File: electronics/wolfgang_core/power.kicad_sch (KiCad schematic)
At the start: 25 parts, among them J1 Battery, J2 Power Supply, U1 LM5001MA, U2 ACS724xLCTR-50AB, U3 LTC4418IUF-PBF

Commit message: More work on CORE Rev2
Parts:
- removed D7: STPS60L30CW, symbol Device:D_Schottky_Dual_CommonCathode_AAK_Parallel
- added C11, C12, C13, C14, C15, C8: C_Small, symbol Device:C_Small
- added C5, C6, C7: C_Polarized_Small, symbol Device:C_Polarized_Small
- added Q1, Q2, Q3, Q4: SUM110P06-08L-E3, symbol Simulation_SPICE:PMOS
- added R11, R12, R13: R_Small, symbol Device:R_Small
- renumbered J2 to J1, J1 to J2
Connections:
- net GND: now also U3.21 (GND), U3.8 (GND), C11.2, C12.2, C13.2, C14.2, C15.2, C5.2, C6.2, C7.2, C8.2, R13.2
- net v_bat: now also R9.1, U3.16 (V2), C7.1, C8.1, Q3.1 (D)
- net v_ext: now also R5.1, U3.17 (V1), C11.1, C6.1, Q1.1 (D)
- net at F1.1: now also U3.15 (V_{OUT}), C5.1, Q2.3 (S), Q4.3 (S), R11.1, R12.1
- net at U3.1 (TMR): now also C14.1
- net at U3.10 (INTV_{CC}): now also U3.18 (EN), U3.9 (CAS), C15.1
- net at U3.11 (G2): now also Q3.2 (G), Q4.2 (G)
- net at U3.12 (VS2): now also C13.1, Q3.3 (S), Q4.1 (D)
- net at U3.13 (G1): now also Q1.2 (G), Q2.2 (G)
- net at U3.14 (VS1): now also C12.1, Q1.3 (S), Q2.1 (D)
- net at U3.20 (HYS): now also R13.1
- net at U3.6 (~{VALID1}): now also R11.2
- net at U3.7 (~{VALID2}): now also R12.2
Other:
- note added: "Note: When contiiung to copy the design, make sure to copy e.g. Figure 10 so that both inputs are hotswappable."
- note added: "TODO: find correct values of the resistors around the LTC44418IUF"
- note removed: "replace with ltc4418"
- moved on the sheet: C1, C10, C2, C3, C4, C9, D8, F1, J1, J2, L1, R1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

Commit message: Further WIP on Power Rev 2.0
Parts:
- C14: value C_Small -> 1nF
- R10, R6: value R_Small -> 2k
- R13: value R_Small -> 0
- R5, R9: value R_Small -> 18k
- R7, R8: value R_Small -> 1k
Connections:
- net GND: now also R7.1, R8.1
- net at C15.1, U3.10 (INTV_{CC}), U3.18 (EN): now also U3.19 (~{SHDN}); no longer U3.9 (CAS)
- no-connect marks 1 -> 2
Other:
- note added: "Note: When continuiung to copy the design, make sure to copy e.g. Figure 10 so that both inputs are hotswappable."
- note added: "Values for V-Div from CIT team. Motivation for exact values unknown They will work, but examples in the datasheet are always a lot bgger (e.g. R5=R9=1M Ohm)"
- note removed: "Note: When contiiung to copy the design, make sure to copy e.g. Figure 10 so that both inputs are hotswappable."
- note removed: "TODO: find correct values of the resistors around the LTC44418IUF"
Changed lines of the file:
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@@
 	)
 	(junction
-		(at 125.73 88.9)
-		(diameter 0)
-		(color 0 0 0 0)
-	)
-	(junction
 		(at 105.41 49.53)
 		(diameter 0)
@@
 	)
 	(junction
-		(at 125.73 85.09)
-		(diameter 0)
-		(color 0 0 0 0)
-	)
-	(junction
 		(at 88.9 186.69)
 		(diameter 0)
@@
 	)
 	(junction
+		(at 125.73 88.9)
+		(diameter 0)
+		(color 0 0 0 0)
+	)
+	(junction
 		(at 270.51 57.15)
 		(diameter 0)
@@
 	)
 	(junction
+		(at 125.73 92.71)
+		(diameter 0)
+		(color 0 0 0 0)
+	)
+	(junction
 		(at 124.46 138.43)
 		(diameter 0)
@@
 		(at 66.04 165.1)
 	)
+	(no_connect
+		(at 125.73 85.09)
+	)
 	(wire
 		(pts
@@
 	(wire
 		(pts
+			(xy 125.73 88.9) (xy 140.97 88.9)
+		)
+		(stroke
+			(width 0)
+			(type default)
+		)
+	)
+	(wire
+		(pts
 			(xy 102.87 114.3) (xy 107.95 114.3)
 		)
@@
 	(wire
 		(pts
+			(xy 140.97 96.52) (xy 140.97 88.9)
+		)
+		(stroke
+			(width 0)
+			(type default)
+		)
+	)
+	(wire
+		(pts
 			(xy 160.02 71.12) (xy 160.02 63.5)
 		)
@@
 	(wire
 		(pts
-			(xy 140.97 85.09) (xy 125.73 85.09)
-		)
-		(stroke
-			(width 0)
-			(type default)
-		)
-	)
-	(wire
-		(pts
 			(xy 134.62 45.72) (xy 140.97 45.72)
 		)
@@
 	(wire
 		(pts
-			(xy 125.73 85.09) (xy 125.73 88.9)
-		)
-		(stroke
-			(width 0)
-			(type default)
-		)
-	)
-	(wire
-		(pts
 			(xy 96.52 138.43) (xy 106.68 138.43)
 		)
@@
 	(wire
 		(pts
-			(xy 124.46 96.52) (xy 125.73 96.52)
+			(xy 246.38 71.12) (xy 247.65 71.12)
 		)
 		(stroke
@@
 	(wire
 		(pts
-			(xy 246.38 71.12) (xy 247.65 71.12)
+			(xy 29.21 25.4) (xy 58.42 25.4)
 		)
 		(stroke
@@
 	(wire
 		(pts
-			(xy 29.21 25.4) (xy 58.42 25.4)
+			(xy 80.01 138.43) (xy 88.9 138.43)
 		)
 		(stroke
@@
 	(wire
 		(pts
-			(xy 80.01 138.43) (xy 88.9 138.43)
+			(xy 87.63 44.45) (xy 87.63 58.42)
 		)
 		(stroke
@@
 	(wire
 		(pts
-			(xy 87.63 44.45) (xy 87.63 58.42)
+			(xy 91.44 109.22) (xy 91.44 114.3)
 		)
 		(stroke
@@
 	(wire
 		(pts
-			(xy 91.44 109.22) (xy 91.44 114.3)
+			(xy 160.02 63.5) (xy 160.02 38.1)
 		)
 		(stroke
@@
 	(wire
 		(pts
-			(xy 160.02 63.5) (xy 160.02 38.1)
+			(xy 125.73 92.71) (xy 125.73 96.52)
 		)
 		(stroke
@@
 	(wire
 		(pts
-			(xy 140.97 96.52) (xy 140.97 85.09)
-		)
-		(stroke
-			(width 0)
-			(type default)
-		)
-	)
-	(wire
-		(pts
 			(xy 146.05 38.1) (xy 160.02 38.1)
 		)
@@
 		)
 	)
-	(text "TODO: find correct values of the resistors around the LTC44418IUF"
+	(text "Supply Selection"
 		(exclude_from_sim no)
-		(at 84.328 124.206 0)
+		(at 59.182 16.51 0)
 		(effects
 			(font
@@
 		)
 	)
-	(text "Supply Selection"
+	(text "Mini ATO Fuse"
 		(exclude_from_sim no)
-		(at 59.182 16.51 0)
+		(at 229.616 29.21 0)
 		(effects
 			(font
@@
 		)
 	)
-	(text "Mini ATO Fuse"
+	(text "Values for V-Div from CIT team.\nMotivation for exact values unknown\nThey will work, but examples in\nthe datasheet are always a lot\nbgger (e.g. R5=R9=1M Ohm)"
 		(exclude_from_sim no)
-		(at 229.616 29.21 0)
+		(at 33.02 84.582 0)
 		(effects
 			(font
@@
 		)
 	)
-	(text "Note: When contiiung to copy the design, make sure to copy e.g. Figure 10 so that both inputs are hotswappable."
+	(text "Note: When continuiung to copy the design, make sure to copy e.g. Figure 10 so that both inputs are hotswappable."
 		(exclude_from_sim no)
 		(at 106.426 126.746 0)
@@
 	)
 	(symbol
+		(lib_id "power:GND")
+		(at 53.34 97.79 270)
+		(unit 1)
+		(exclude_from_sim no)
+		(in_bom yes)
+		(on_board yes)
+		(dnp no)
+		(fields_autoplaced yes)
+		(property "Reference" "#PWR036"
+			(at 46.99 97.79 0)
+			(effects
+				(font
+					(size 1.27 1.27)
+				)
+				(hide yes)
+			)
+		)
+		(property "Value" "GND"
+			(at 49.53 97.7899 90)
+			(effects
+				(font
+					(size 1.27 1.27)
+				)
+				(justify right)
+			)
+		)
+		(property "Footprint" ""
+			(at 53.34 97.79 0)
+			(effects
+				(font
+					(size 1.27 1.27)
+				)
+				(hide yes)
+			)
+		)
+		(property "Datasheet" ""
+			(at 53.34 97.79 0)
+			(effects
+				(font
+					(size 1.27 1.27)
+				)
+				(hide yes)
+			)
+		)
+		(property "Description" "Power symbol creates a global label with name \"GND\" , ground"
+			(at 53.34 97.79 0)
+			(effects
+				(font
+					(size 1.27 1.27)
+				)
+				(hide yes)
+			)
+		)
+		(pin "1"
+		)
+		(instances
+			(project "wolfgang_core"
+				(path "/9538e4ed-27e6-4c37-b989-9859dc0d49e8/03085433-09a6-46e6-a151-340cb0e29306"
+					(reference "#PWR036")
+					(unit 1)
+				)
+			)
+		)
+	)
+	(symbol
 		(lib_id "Connector_Generic:Conn_01x02")
 		(at 24.13 40.64 0)
@@
 			)
 		)
-		(property "Value" "R_Small"
+		(property "Value" "1k"
 			(at 69.85 83.312 90)
 			(effects
@@
 			)
 		)
-		(property "Value" "R_Small"
+		(property "Value" "18k"
 			(at 61.976 90.17 0)
 			(effects
@@
 			)
 		)
-		(property "Value" "R_Small"
+		(property "Value" "2k"
 			(at 75.946 78.74 0)
 			(effects
@@
 			)
 		)
-		(property "Value" "R_Small"
+		(property "Value" "2k"
 			(at 61.976 95.25 0)
 			(effects
@@
 			)
 		)
-		(property "Value" "R_Small"
+		(property "Value" "18k"
 			(at 75.946 73.66 0)
 			(effects
@@
 	(symbol
 		(lib_id "power:GND")
+		(at 67.31 81.28 270)
+		(unit 1)
+		(exclude_from_sim no)
+		(in_bom yes)
+		(on_board yes)
+		(dnp no)
+		(fields_autoplaced yes)
+		(property "Reference" "#PWR035"
+			(at 60.96 81.28 0)
+			(effects
+				(font
+					(size 1.27 1.27)
+				)
+				(hide yes)
+			)
+		)
+		(property "Value" "GND"
+			(at 63.5 81.2799 90)
+			(effects
+				(font
+					(size 1.27 1.27)
+				)
+				(justify right)
+			)
+		)
+		(property "Footprint" ""
+			(at 67.31 81.28 0)
+			(effects
+				(font
+					(size 1.27 1.27)
+				)
+				(hide yes)
+			)
+		)
+		(property "Datasheet" ""
+			(at 67.31 81.28 0)
+			(effects
+				(font
+					(size 1.27 1.27)
+				)
+				(hide yes)
+			)
+		)
+		(property "Description" "Power symbol creates a global label with name \"GND\" , ground"
+			(at 67.31 81.28 0)
+			(effects
+				(font
+					(size 1.27 1.27)
+				)
+				(hide yes)
+			)
+		)
+		(pin "1"
+		)
+		(instances
+			(project "wolfgang_core"
+				(path "/9538e4ed-27e6-4c37-b989-9859dc0d49e8/03085433-09a6-46e6-a151-340cb0e29306"
+					(reference "#PWR035")
+					(unit 1)
+				)
+			)
+		)
+	)
+	(symbol
+		(lib_id "power:GND")
 		(at 72.39 58.42 0)
 		(unit 1)
@@
 		(on_board yes)
 		(dnp no)
-		(fields_autoplaced yes)
 		(property "Reference" "C14"
-			(at 110.49 110.4962 0)
+			(at 108.712 109.982 0)
 			(effects
 				(font
@@
 			)
 		)
-		(property "Value" "C_Small"
-			(at 110.49 113.0362 0)
+		(property "Value" "1nF"
+			(at 108.966 113.03 0)
 			(effects
 				(font
@@
 		(on_board yes)
 		(dnp no)
-		(fields_autoplaced yes)
 		(property "Reference" "R13"
-			(at 105.41 110.4899 0)
+			(at 100.838 113.792 90)
 			(effects
 				(font
@@
 			)
 		)
-		(property "Value" "R_Small"
-			(at 105.41 113.0299 0)
+		(property "Value" "0"
+			(at 104.902 113.792 90)
 			(effects
 				(font
@@
 			)
 		)
-		(property "Value" "R_Small"
+		(property "Value" "1k"
 			(at 55.88 99.822 90)
 			(effects

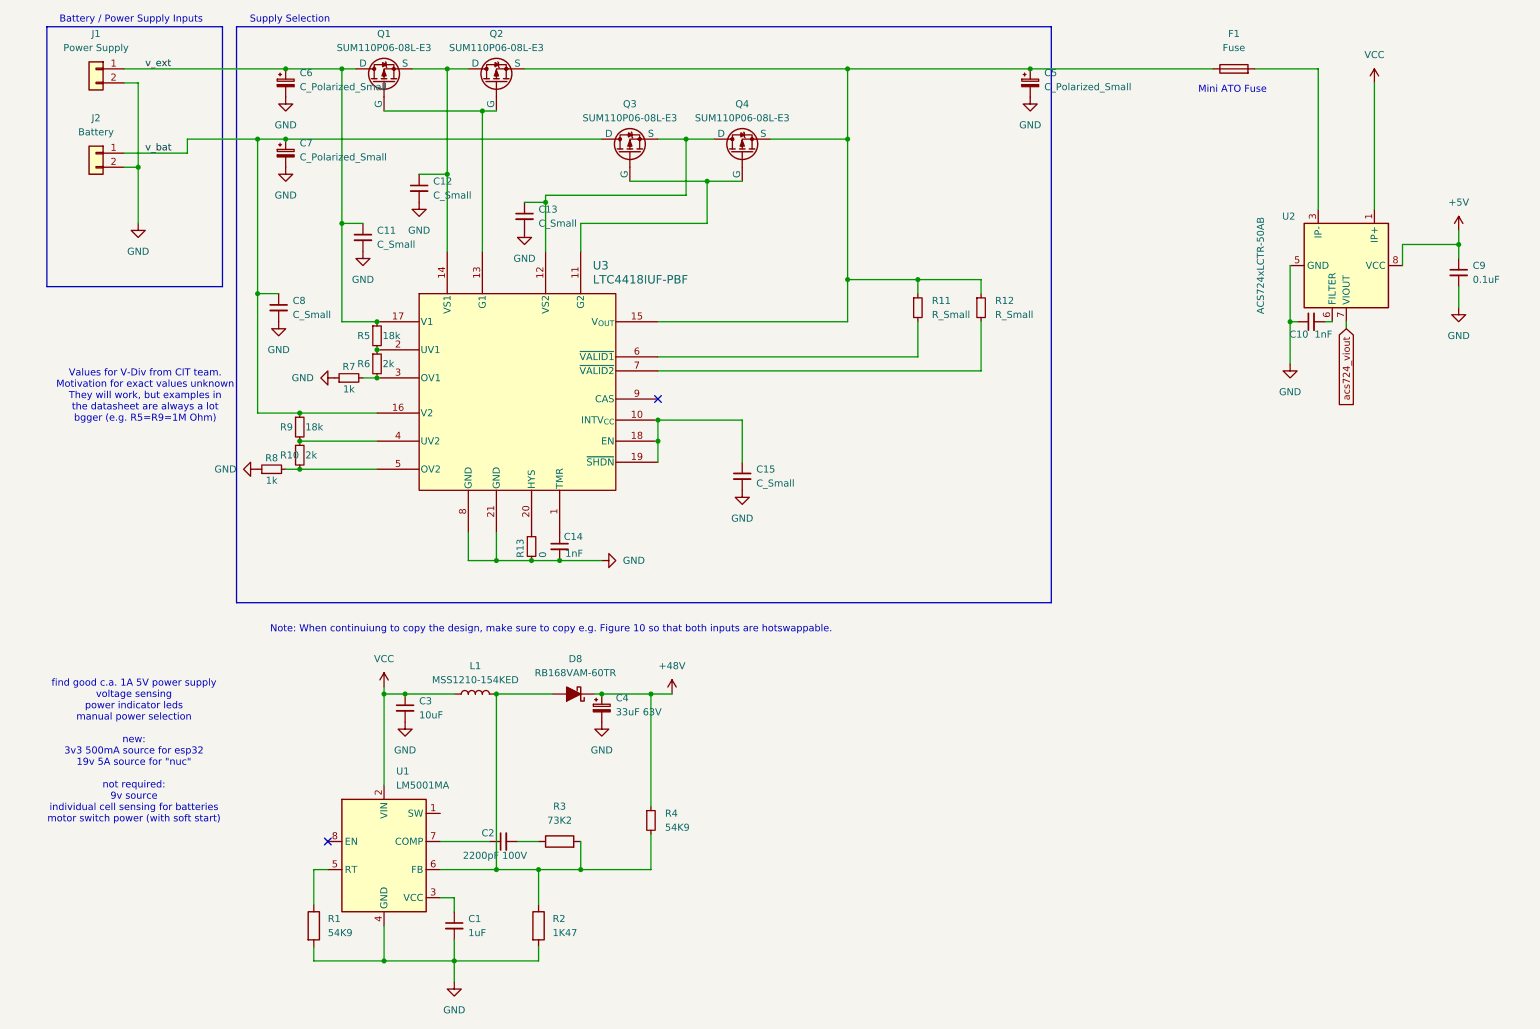
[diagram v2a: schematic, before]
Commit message: Add ESD protection diode, add footprints
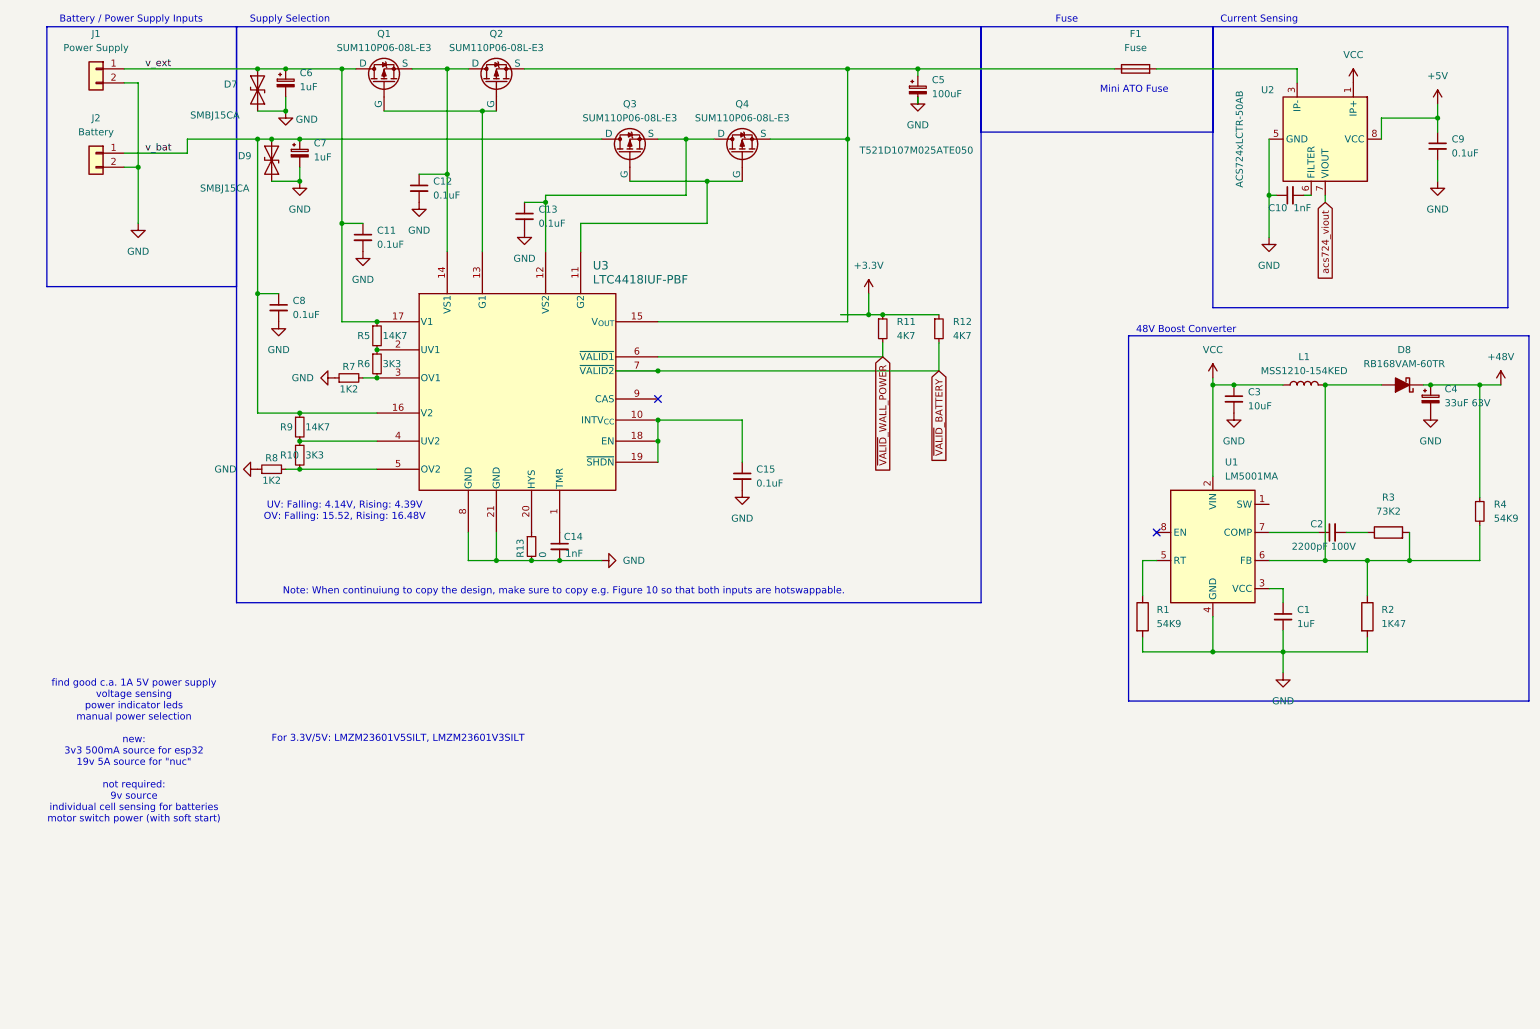
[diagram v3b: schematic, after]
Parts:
- added D7, D9: SMBJ15CA, footprints:DIONM5436X244N, symbol Diode:SD15_SOD323
- C11, C12, C13, C15, C8: value C_Small -> 0.1uF
- C5: value C_Polarized_Small -> 100uF; footprint (none) -> footprints:T521D; Part# (none) -> T521D107M025ATE050
- C6, C7: value C_Polarized_Small -> 1uF
- R10, R6: value 2k -> 3K3
- R11, R12: value R_Small -> 4K7
- R5, R9: value 18k -> 14K7
- R7, R8: value 1k -> 1K2
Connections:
- net GND: now also D7.1 (A1), D9.1 (A1)
- net v_bat: now also D9.2 (A2)
- net v_ext: now also D7.2 (A2)
- net at C5.1, F1.1, Q2.3 (S)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: no longer R11.1, R12.1
- net ~{VALID}_WALL_POWER: now reaches R11.2, U3.6 (~{VALID1})
- net ~{VALID}_BATTERY: now reaches R12.2, U3.7 (~{VALID2})
- new net +3.3V: R11.1, R12.1
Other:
- note added: "48V Boost Converter"
- note added: "Current Sensing"
- note added: "For 3.3V/5V: LMZM23601V5SILT, LMZM23601V3SILT"
- note added: "Fuse"
- note added: "UV: Falling: 4.14V, Rising: 4.39V OV: Falling: 15.52, Rising: 16.48V"
- note removed: "Values for V-Div from CIT team. Motivation for exact values unknown They will work, but examples in the datasheet are always a lot bgger (e.g. R5=R9=1M Ohm)"
- moved on the sheet: C1, C10, C2, C3, C4, C5, C7, C9, D8, F1, L1, R1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

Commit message: Updated a Note
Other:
- note added: "For 3.3V/5V: VXO7803-500-M-TR or ROF-78E5.0-0.5SMD-R"
- note removed: "For 3.3V/5V: LMZM23601V5SILT, LMZM23601V3SILT"
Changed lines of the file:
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@@
 		)
 	)
-	(text "For 3.3V/5V: LMZM23601V5SILT, LMZM23601V3SILT"
+	(text "For 3.3V/5V: VXO7803-500-M-TR or ROF-78E5.0-0.5SMD-R "
 		(exclude_from_sim no)
 		(at 78.74 146.558 0)
